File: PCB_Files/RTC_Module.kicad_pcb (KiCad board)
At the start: 2 copper layers, 33 x 19.6 mm, 15 parts, among them J1 DZ254W-11-06-65, U1 DS3231SN#T&R, U2 AMS1117-3.3

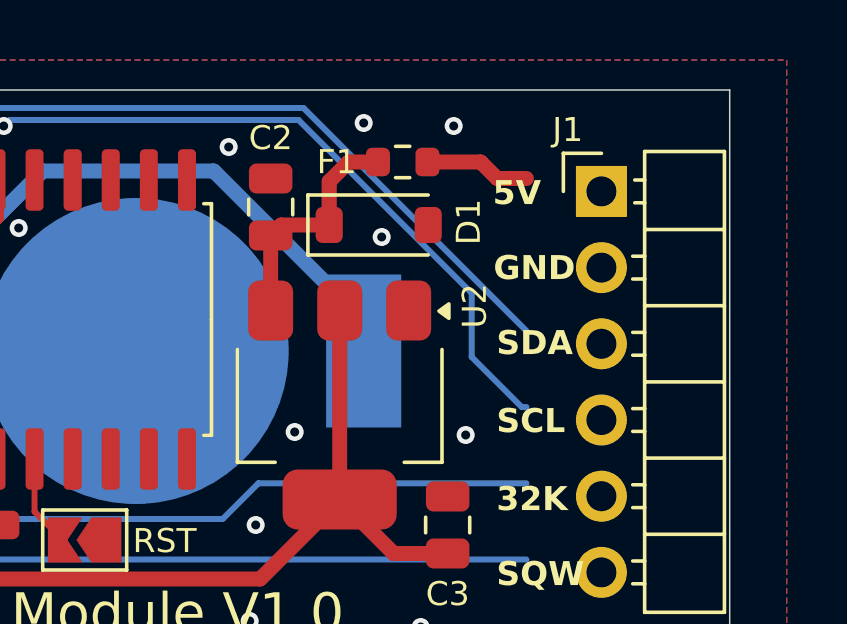
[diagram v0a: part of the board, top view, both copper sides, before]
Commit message: Added new RTC that is much cheaper.
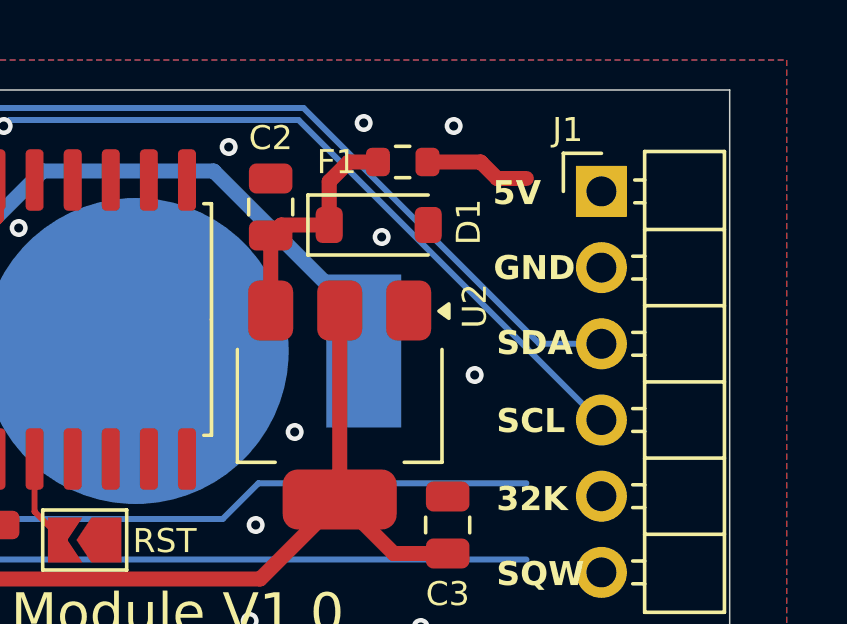
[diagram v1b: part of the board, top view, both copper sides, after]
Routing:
- net /SDA: track 29.6 -> 32.3 mm
- net /SCL: track 30.4 -> 31.8 mm
- net GND: vias 15 -> 14
- net (no net): vias 0 -> 1
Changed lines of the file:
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@@
 			(pinfunction "Pin_2")
 			(pintype "passive")
+			(zone_connect 1)
 		)
 		(pad "3" thru_hole oval
@@
 		)
 		(property "Value" "22uF/10V"
-			(at 0 1.679999 270)
+			(at 0 1.679999 -90)
 			(layer "F.Fab")
 			(effects
@@
 		)
 		(fp_text user "${REFERENCE}"
-			(at 0 0 270)
+			(at 0 0 -90)
 			(layer "F.Fab")
 			(effects
@@
 		)
 		(property "Value" "MM1Z4V7"
-			(at 0 2.1 360)
+			(at 0 2.1 0)
 			(layer "F.Fab")
 			(effects
@@
 		)
 		(fp_text user "${REFERENCE}"
-			(at 0 -2.000001 360)
+			(at 0 -2.000001 0)
 			(layer "F.Fab")
 			(effects
@@
 		)
 		(property "Value" "4k7"
-			(at 0 1.43 360)
+			(at 0 1.43 0)
 			(layer "F.Fab")
 			(effects
@@
 		)
 		(fp_text user "${REFERENCE}"
-			(at 0 0 360)
+			(at 0 0 0)
 			(layer "F.Fab")
 			(effects
@@
 		)
 		(property "Value" "4k7"
-			(at 0 1.43 360)
+			(at 0 1.43 0)
 			(layer "F.Fab")
 			(effects
@@
 		)
 		(fp_text user "${REFERENCE}"
-			(at 0 0 360)
+			(at 0 0 0)
 			(layer "F.Fab")
 			(effects
@@
 		)
 		(property "Value" "10uF/10V"
-			(at 0 1.679999 270)
+			(at 0 1.679999 -90)
 			(layer "F.Fab")
 			(effects
@@
 		)
 		(fp_text user "${REFERENCE}"
-			(at 0 0 270)
+			(at 0 0 -90)
 			(layer "F.Fab")
 			(effects
@@
 		)
 		(property "Value" "4k7"
-			(at 0 1.43 360)
+			(at 0 1.43 0)
 			(layer "F.Fab")
 			(effects
@@
 		)
 		(fp_text user "${REFERENCE}"
-			(at 0 0 360)
+			(at 0 0 0)
 			(layer "F.Fab")
 			(effects
@@
 		)
 		(property "Value" "4k7"
-			(at 0 1.43 360)
+			(at 0 1.43 0)
 			(layer "F.Fab")
 			(effects
@@
 		)
 		(fp_text user "${REFERENCE}"
-			(at 0 0 360)
+			(at 0 0 0)
 			(layer "F.Fab")
 			(effects
@@
 	)
 	(via
+		(at 153.6 69)
+		(size 0.6)
+		(drill 0.3)
+		(layers "F.Cu" "B.Cu")
+		(net 0)
+	)
+	(via
 		(at 132.5 62.2)
 		(size 0.6)
@@
 	)
 	(via
-		(at 153.3 71)
-		(size 0.6)
-		(drill 0.3)
-		(layers "F.Cu" "B.Cu")
-		(free yes)
-		(net 1)
-	)
-	(via
 		(at 149.9 60.6)
 		(size 0.6)
@@
 	)
 	(segment
-		(start 147.895 60.1)
-		(end 155.325 67.53)
+		(start 137.6 60.1)
+		(end 147.895 60.1)
 		(width 0.2)
 		(layer "B.Cu")
@@
 	)
 	(segment
-		(start 137.6 60.1)
-		(end 147.895 60.1)
+		(start 155.755 67.96)
+		(end 157.825 67.96)
+		(width 0.2)
+		(layer "B.Cu")
+		(net 5)
+	)
+	(segment
+		(start 147.895 60.1)
+		(end 155.755 67.96)
 		(width 0.2)
 		(layer "B.Cu")
@@
 	)
 	(segment
-		(start 153.5 66.270686)
-		(end 153.5 68.4)
+		(start 137.9 60.7)
+		(end 138.1 60.5)
 		(width 0.2)
 		(layer "B.Cu")
@@
 	)
 	(segment
-		(start 155.17 70.07)
-		(end 155.325 70.07)
+		(start 147.729314 60.5)
+		(end 157.729314 70.5)
 		(width 0.2)
 		(layer "B.Cu")
@@
 	)
 	(segment
-		(start 137.9 60.7)
-		(end 138.1 60.5)
-		(width 0.2)
-		(layer "B.Cu")
-		(net 8)
-	)
-	(segment
-		(start 153.5 68.4)
-		(end 155.17 70.07)
-		(width 0.2)
-		(layer "B.Cu")
-		(net 8)
-	)
-	(segment
-		(start 147.729314 60.5)
-		(end 153.5 66.270686)
+		(start 157.729314 70.5)
+		(end 157.825 70.5)
 		(width 0.2)
 		(layer "B.Cu")

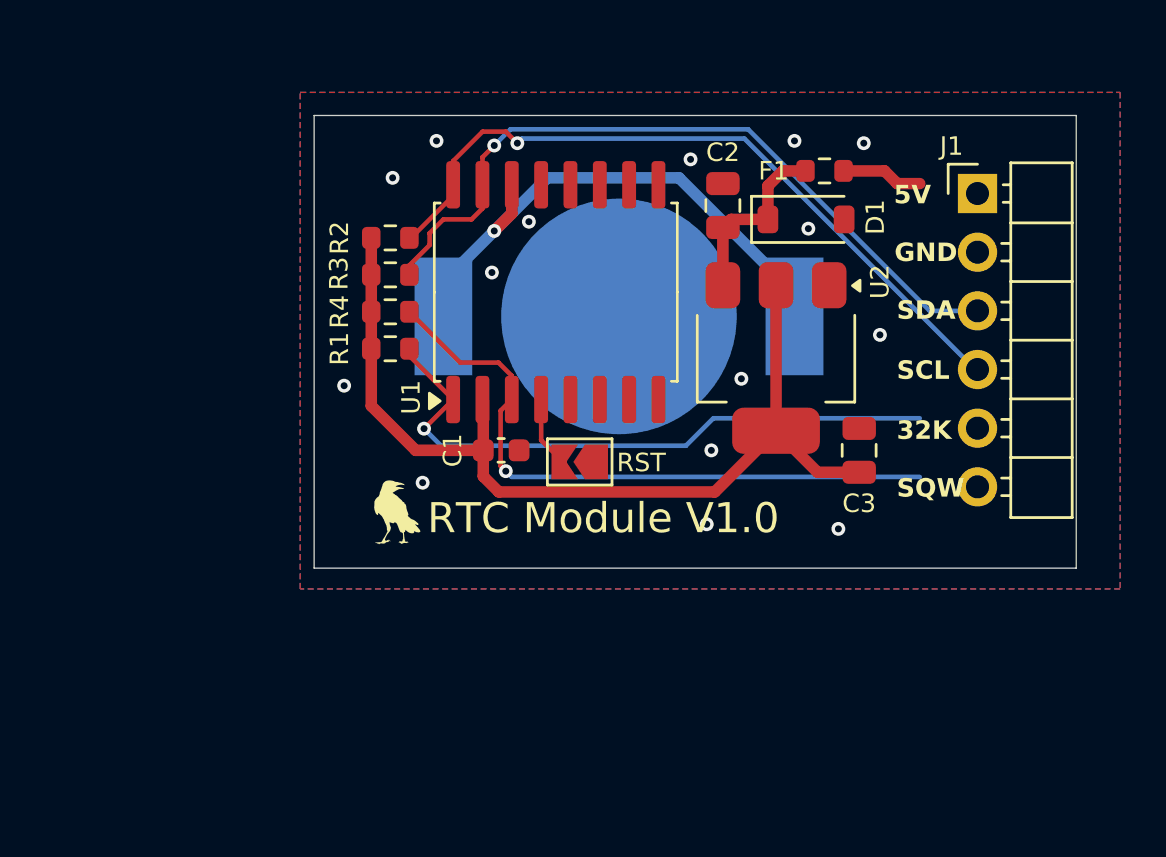
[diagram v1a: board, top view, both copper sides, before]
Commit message: Finished PCB with new RTC.
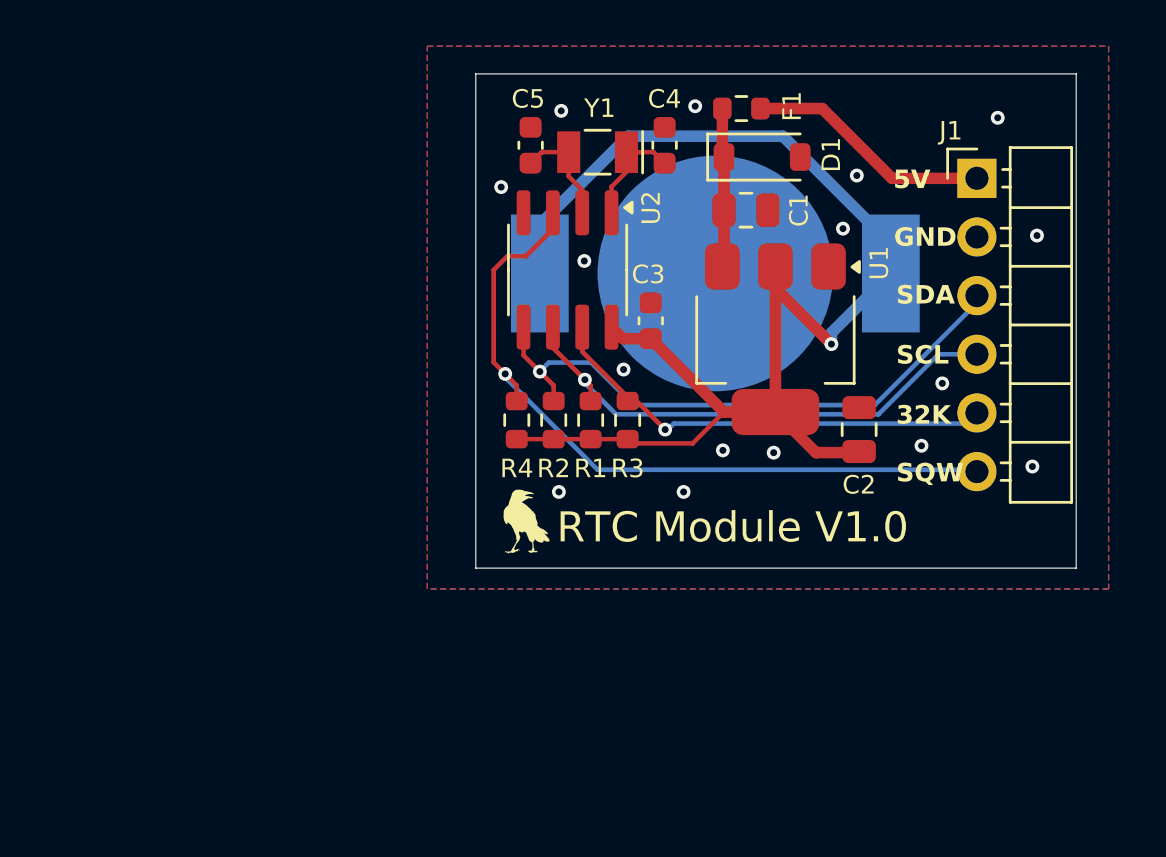
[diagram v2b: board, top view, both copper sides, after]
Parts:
- removed the C1 at (137.2, 74.0)
- removed JP1: SolderJumper_2_Open, Jumper:SolderJumper-2_P1.3mm_Open_TrianglePad1.0x1.5mm
- removed the U1 at (139.6, 67.2)
- added C3: 100nF/10V, Capacitor_SMD:C_0603_1608Metric, F.Cu at (143.7, 68.4)
- added C4: 12p5/10V, Capacitor_SMD:C_0603_1608Metric, F.Cu at (144.3, 60.8)
- added C5: 12p5/10V, Capacitor_SMD:C_0603_1608Metric, F.Cu at (138.5, 60.8)
- added U2: PCF8563T, Package_SO:SOIC-8_3.9x4.9mm_P1.27mm, F.Cu at (140.1, 66.2)
- added Y1: Q13FC13500004, Crystal:Crystal_SMD_MicroCrystal_CC7V-T1A-2Pin_3.2x1.5mm, F.Cu at (141.4, 61.1)
- moved R3 12.0 mm to (142.7, 72.7), turned to 90 degrees
- moved R2 10.6 mm to (139.5, 72.7), turned to 90 degrees
- moved R1 9.21 mm to (141.1, 72.7), turned to 90 degrees
- moved R4 7.21 mm to (137.9, 72.7), turned to 90 degrees
- moved G*** 5.61 mm to (138.3, 77.1)
- moved BT1 4.57 mm to (146.5, 66.3), turned to 180 degrees
- moved F1 4.50 mm to (147.6, 59.2)
- moved D1 3.30 mm to (148.5, 61.3)
- moved C1 1.02 mm to (147.8, 63.6), turned to 0 degrees
- moved C2 0.90 mm to (152.7, 73.1)
- moved U1 0.81 mm to (149.1, 69.2)
- moved J1 0.66 mm to (157.8, 62.2)
- renumbered C2 to C1, C3 to C2, U2 to U1
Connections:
- net /SQW renamed /INT
- BT1 pad 1: Net-(BT1-+) -> 3.3V
- J1 pad 5: /32KHZ -> /CLK
- R1 pad 2: /32KHZ -> /SCL
- R2 pad 2: /SCL -> /SDA
- R3 pad 2: /SDA -> /CLK
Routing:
- net /32KHZ: track 27.0 -> 0.00 mm, vias 1 -> 0
- net Net-(BT1-+): track 23.9 -> 0.00 mm, vias 1 -> 0
- net /CLK: track 0.00 -> 19.9 mm, vias 0 -> 1
- net 3.3V: track 41.0 -> 59.5 mm, vias 0 -> 1
- net /SCL: track 31.8 -> 22.5 mm
- net 5V: track 3.53 -> 10.6 mm
- net /SDA: track 32.3 -> 25.9 mm
- net /OSCO: track 0.00 -> 5.12 mm
- net /OSCI: track 0.00 -> 5.09 mm
- net /INT: track 28.0 -> 32.2 mm
- net /RST: track 3.09 -> 0.00 mm
- net Net-(D1-K): track 7.94 -> 6.90 mm
- net GND: vias 14 -> 16
- net (no net): vias 1 -> 0
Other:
- board size 33 x 19.6 mm -> 26 x 21.4 mm
- board text removed: "RST"

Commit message: Added step of DCDC. Updated gitignore. Now version with battery cell on top side.
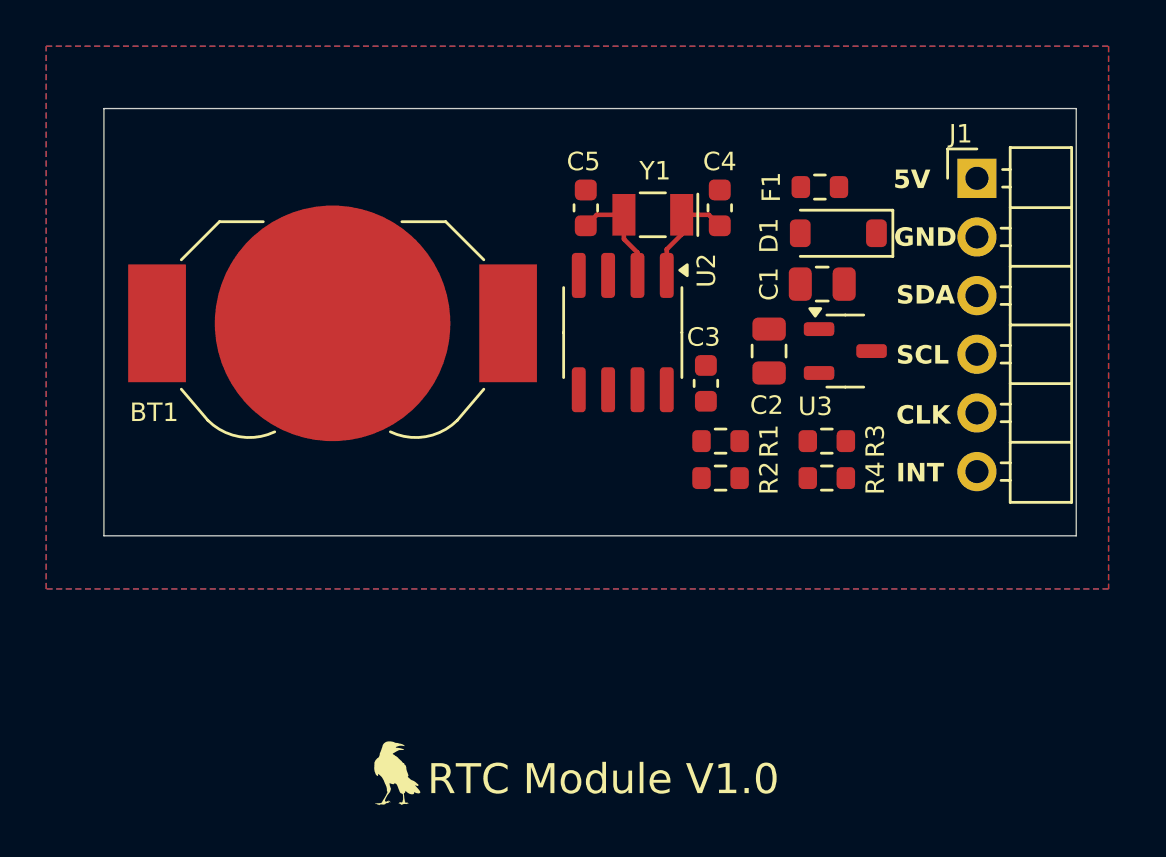
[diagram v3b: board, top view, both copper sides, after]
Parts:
- removed U1: AMS1117-3.3, Package_TO_SOT_SMD:SOT-223-3_TabPin2
- added U3: XC6206PxxxMR, Package_TO_SOT_SMD:SOT-23-3, F.Cu at (152.1, 69.7)
- BT1: moved to F.Cu
- C1: value 10uF/10V -> 1uF/10V
- C2: value 22uF/10V -> 1uF/10V
- moved BT1 16.7 mm to (129.9, 68.5), turned to 0 degrees
- moved R4 13.7 mm to (151.3, 75.2), turned to 180 degrees
- moved G*** 12.3 mm to (132.7, 88.0)
- moved R3 8.67 mm to (151.3, 73.6), turned to 180 degrees
- moved R2 7.65 mm to (146.7, 75.2), turned to 180 degrees
- moved R1 5.70 mm to (146.7, 73.6), turned to 180 degrees
- moved C2 5.17 mm to (148.8, 69.7)
- moved F1 4.81 mm to (151.0, 62.6)
- moved D1 4.67 mm to (151.8, 64.6), turned to 180 degrees
- moved C1 4.60 mm to (151.1, 66.8), turned to 180 degrees
- moved U2 3.61 mm to (142.5, 68.9)
- moved C5 3.61 mm to (140.9, 63.5)
- moved C4 3.61 mm to (146.7, 63.5)
- moved C3 3.61 mm to (146.1, 71.1)
- moved Y1 3.61 mm to (143.8, 63.8)
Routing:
- net 3.3V: track 59.5 -> 0.00 mm, vias 1 -> 0
- net /INT: track 32.2 -> 0.00 mm, vias 1 -> 0
- net /SDA: track 25.9 -> 0.00 mm, vias 1 -> 0
- net /SCL: track 22.5 -> 0.00 mm, vias 1 -> 0
- net /CLK: track 19.9 -> 0.00 mm, vias 1 -> 0
- net 5V: track 10.6 -> 0.00 mm
- net Net-(D1-K): track 6.90 -> 0.00 mm
- net GND: vias 16 -> 0
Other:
- board size 26 x 21.4 mm -> 42.1 x 18.5 mm
- board text added: "CLK"
- board text added: "INT"
- board text removed: "32K"
- board text removed: "SQW"

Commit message: Finished with only Top Side Components.
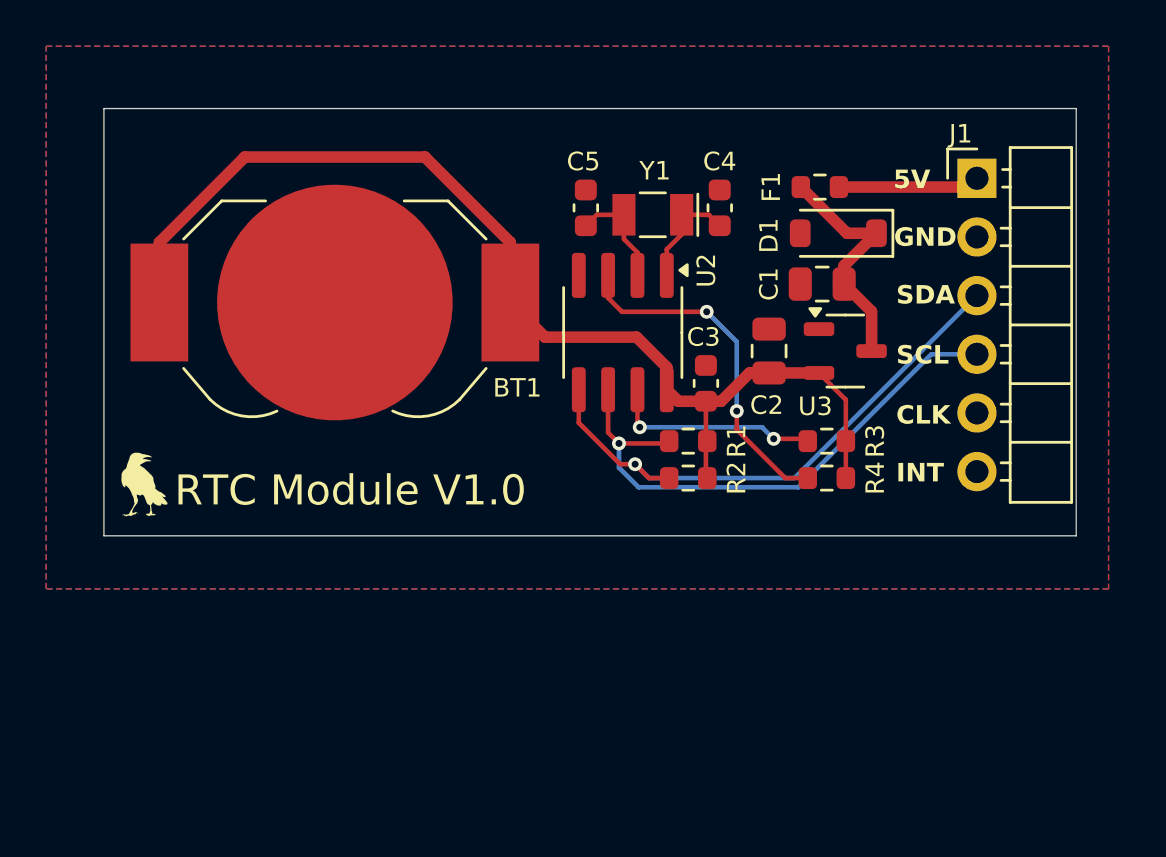
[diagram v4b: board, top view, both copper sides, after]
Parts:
- moved G*** 16.6 mm to (121.8, 75.5)
- moved R1 1.40 mm to (145.3, 73.6)
- moved R2 1.40 mm to (145.3, 75.2)
- moved BT1 0.91 mm to (130.0, 67.6)
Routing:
- net 3.3V: track 0.00 -> 49.4 mm
- net /SDA: track 0.00 -> 24.7 mm, vias 0 -> 1
- net /SCL: track 0.00 -> 24.0 mm, vias 0 -> 1
- net /INT: track 0.00 -> 15.1 mm, vias 0 -> 2
- net Net-(D1-K): track 0.00 -> 10.3 mm
- net /CLK: track 0.00 -> 9.19 mm, vias 0 -> 2
- net 5V: track 0.00 -> 6.13 mm

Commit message: Now finished and choose SMD battery.
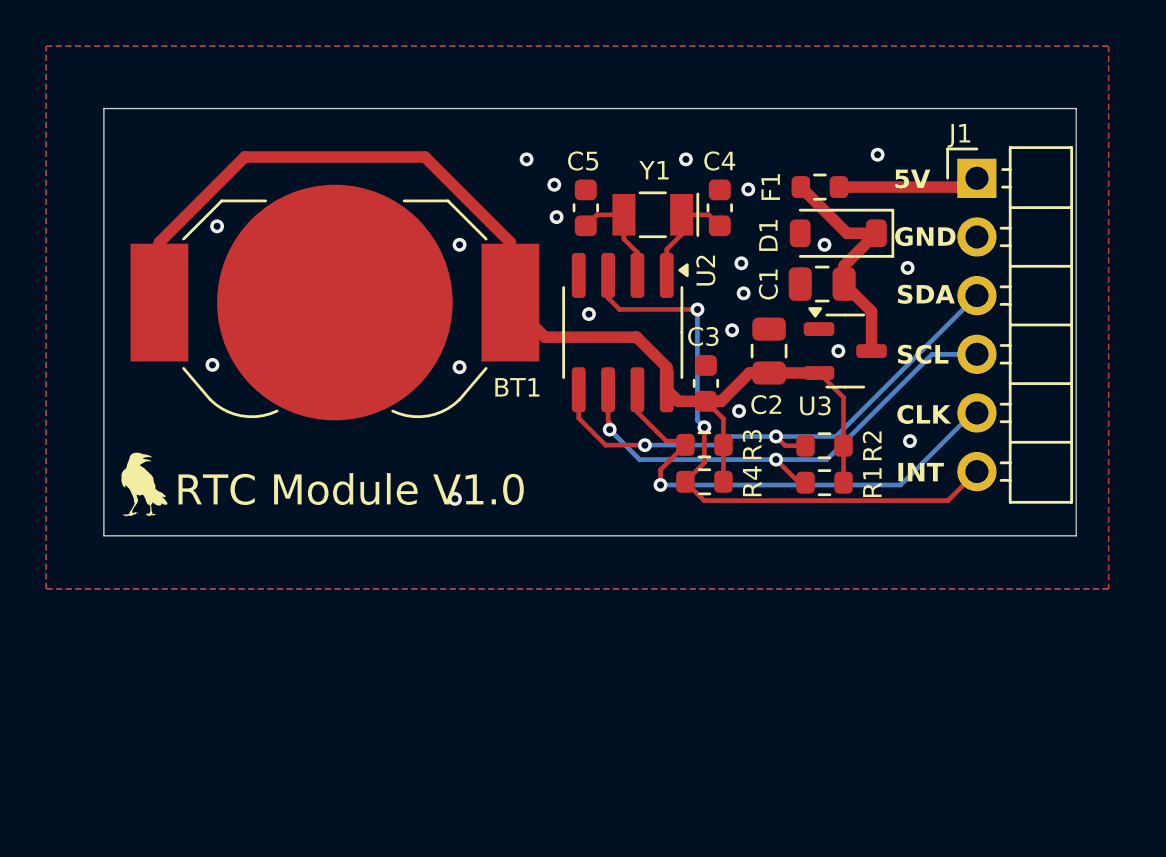
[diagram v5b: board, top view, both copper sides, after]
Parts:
- moved R1 6.17 mm to (151.2, 75.4)
- moved R2 6.06 mm to (151.2, 73.8)
- moved R3 5.30 mm to (146.0, 73.8)
- moved R4 5.30 mm to (146.0, 75.4)
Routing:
- net /CLK: track 9.19 -> 20.7 mm, vias 2 -> 1
- net /INT: track 15.1 -> 26.6 mm
- net /SCL: track 24.0 -> 21.8 mm, vias 1 -> 2
- net /SDA: track 24.7 -> 23.1 mm, vias 1 -> 2
- net 3.3V: track 49.4 -> 49.9 mm
- net GND: vias 0 -> 20

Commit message: This is ordered Version!!!!
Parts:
- BT1: value Battery_Cell -> MY-1220-03
- U3: value XC6206PxxxMR -> XC6206P332MR-G
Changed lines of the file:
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@@
 			)
 		)
-		(property "Value" "Battery_Cell"
+		(property "Value" "MY-1220-03"
 			(at 0 -6.999999 360)
 			(layer "F.Fab")
@@
 			)
 		)
-		(property "Value" "XC6206PxxxMR"
+		(property "Value" "XC6206P332MR-G"
 			(at 0 2.4 360)
 			(layer "F.Fab")
